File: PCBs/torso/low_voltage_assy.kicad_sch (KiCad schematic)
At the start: 23 parts, among them J3 Conn_01x03, U3 LM317_TO-220, U4 LM317_TO-220

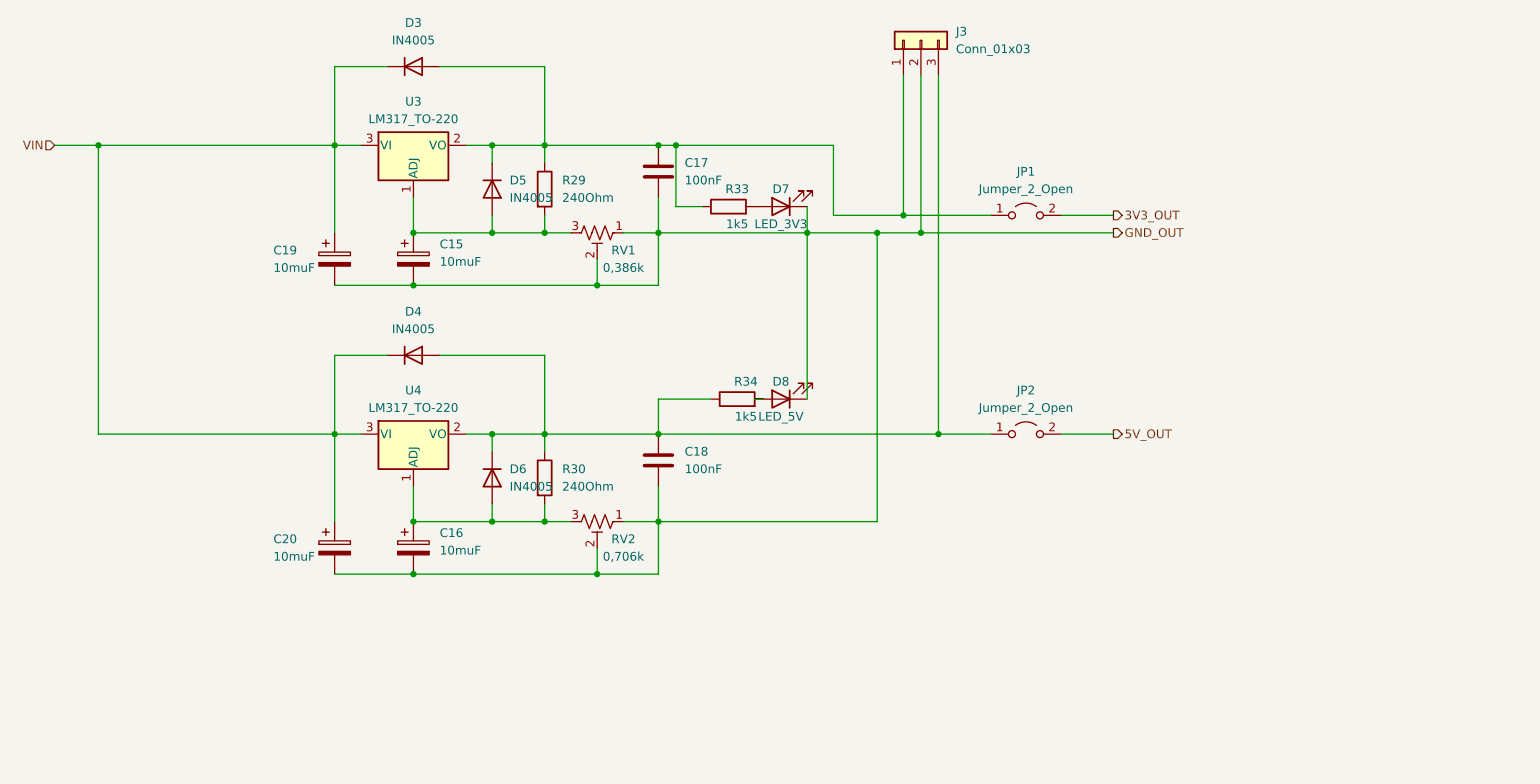
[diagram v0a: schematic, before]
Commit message: Torso all but complete, making bogie before checking the last mark
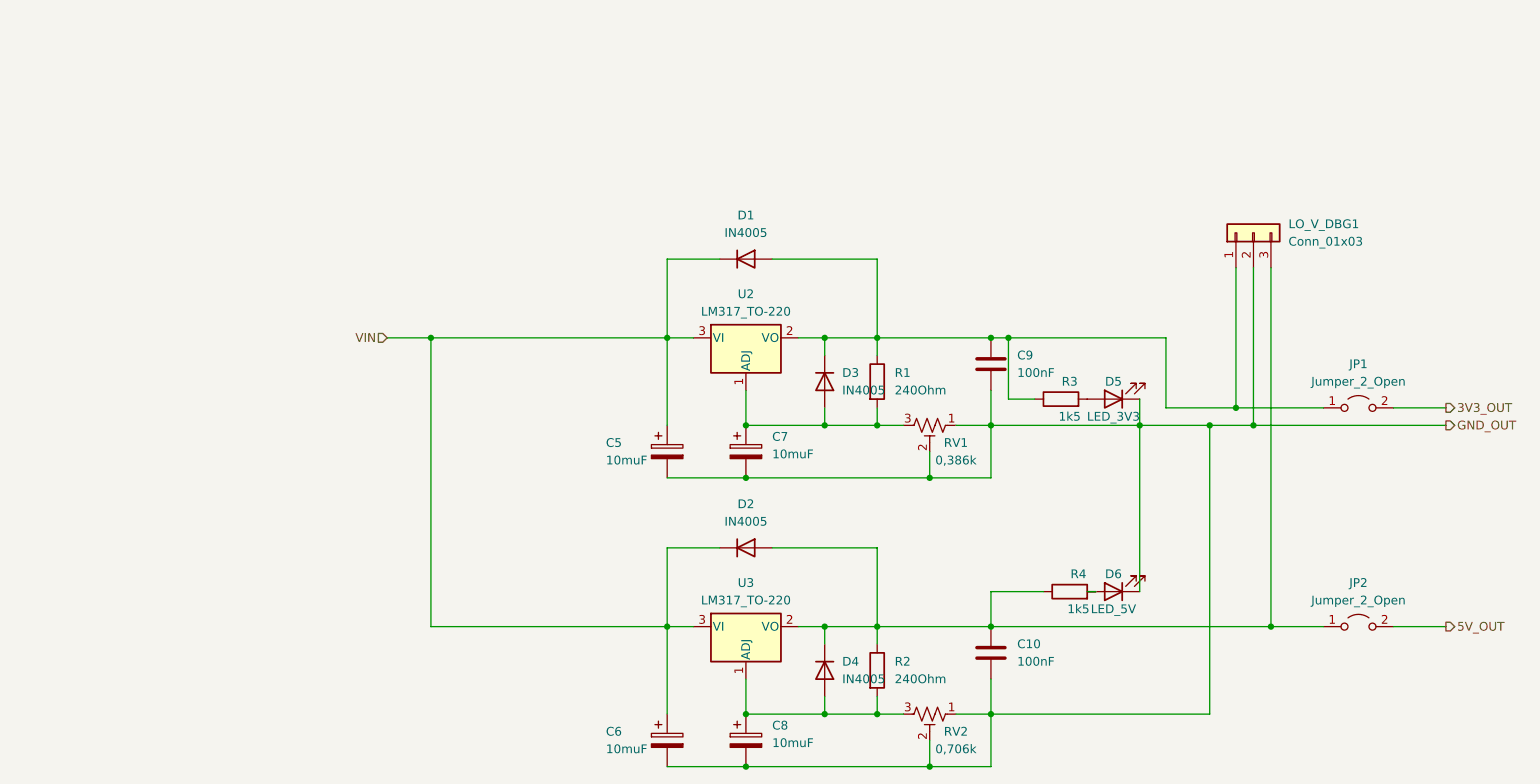
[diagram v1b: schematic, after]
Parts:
- removed C15, C16, C19, C20: 10muF, Capacitor_THT:CP_Radial_D5.0mm_P2.00mm, symbol Device:C_Polarized
- removed C17, C18: 100nF, Capacitor_SMD:C_0603_1608Metric, symbol Device:C
- removed D5, D6: IN4005, Diode_THT:D_T-1_P5.08mm_Horizontal, symbol Device:D
- removed D7: LED_3V3, LED_SMD:LED_0603_1608Metric, symbol Device:LED
- removed D8: LED_5V, LED_SMD:LED_0603_1608Metric, symbol Device:LED
- removed J3: Conn_01x03, Connector_PinHeader_2.54mm:PinHeader_1x03_P2.54mm_Vertical, symbol Connector_Generic:Conn_01x03
- removed R29, R30: 240Ohm, Resistor_SMD:R_0805_2012Metric, symbol Device:R
- removed R33, R34: 1k5, Resistor_SMD:R_0805_2012Metric, symbol Device:R
- removed U4: LM317_TO-220, Package_TO_SOT_THT:TO-220-3_Vertical, symbol Regulator_Linear:LM317_TO-220
- added C10, C9: 100nF, Capacitor_SMD:C_0603_1608Metric, symbol Device:C
- added C5, C6, C7, C8: 10muF, Capacitor_THT:CP_Radial_D5.0mm_P2.00mm, symbol Device:C_Polarized
- added D1, D2: IN4005, Diode_THT:D_T-1_P5.08mm_Horizontal, symbol Device:D
- added D5: LED_3V3, LED_SMD:LED_0603_1608Metric, symbol Device:LED
- added D6: LED_5V, LED_SMD:LED_0603_1608Metric, symbol Device:LED
- added LO_V_DBG1: Conn_01x03, Connector_PinHeader_2.54mm:PinHeader_1x03_P2.54mm_Vertical, symbol Connector_Generic:Conn_01x03
- added R1, R2: 240Ohm, Resistor_SMD:R_0805_2012Metric, symbol Device:R
- added R3, R4: 1k5, Resistor_SMD:R_0805_2012Metric, symbol Device:R
- added U2: LM317_TO-220, Package_TO_SOT_THT:TO-220-3_Horizontal_TabDown, symbol Regulator_Linear:LM317_TO-220
- U3: footprint Package_TO_SOT_THT:TO-220-3_Vertical -> Package_TO_SOT_THT:TO-220-3_Horizontal_TabDown
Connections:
- net GND_OUT: now also C10.2, C5.2, C6.2, C7.2, C8.2, C9.2, D5.1 (K), D6.1 (K), LO_V_DBG1.2 (Pin_2)
- net VIN: now also C5.1, C6.1, D1.1 (K), D2.1 (K), U2.3 (VI); no longer D3.1 (K), D4.1 (K)
- net at U3.1 (ADJ): now also D4.2 (A), RV2.3, C8.1, R2.2; no longer RV1.3
- net at JP2.1 (A): now also D4.1 (K), U3.2 (VO), C10.1, D2.2 (A), LO_V_DBG1.3 (Pin_3), R2.1, R4.1; no longer D4.2 (A)
- new net: C9.1, D1.2 (A), D3.1 (K), JP1.1 (A), LO_V_DBG1.1 (Pin_1), R1.1, R3.1, U2.2 (VO)
- new net: D5.2 (A), R3.2
- new net: C7.1, D3.2 (A), R1.2, RV1.3, U2.1 (ADJ)
- new net: D6.2 (A), R4.2
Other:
- title: Low voltage assembly -> (none)

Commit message: merged changes from timertests, mostly documentation and such. Did not add tim6 config
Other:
- title: (none) -> Low voltage assembly
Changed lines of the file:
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@@
 (kicad_sch (version 20230121) (generator eeschema)
   (paper "A4")
+  (title_block
+    (title "Low voltage assembly")
+    (rev "Mk1.2")
+  )
   (junction (at 161.29 118.11) (diameter 0) (color 0 0 0 0)
   )
